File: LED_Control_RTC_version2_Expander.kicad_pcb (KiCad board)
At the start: 4 copper layers, 100 x 60 mm, 90 parts, among them J10 Conn_01x06_Male, J210 Conn_01x02, J220 Conn_01x02, J230 Conn_01x02, J240 Conn_01x02, J250 Conn_01x02, J260 Conn_01x02, J3 Conn_02x04_Odd_Even, J4 DS1023-2*8SF11, J5 DS1023-2*8SF11, J9 Conn_01x06_Male, Q1 IRLR8726TRPBF, Q10 IRLR8726TRPBF, Q2 IRLR8726TRPBF, Q3 IRLR8726TRPBF, Q4 IRLR8726TRPBF, Q5 IRLR8726TRPBF, Q6 IRLR8726TRPBF, Q7 IRLR8726TRPBF, Q8 IRLR8726TRPBF, Q9 IRLR8726TRPBF, U101 TC4427, U102 TC4427, U103 TC4427, U104 TC4427, U105 TC4427

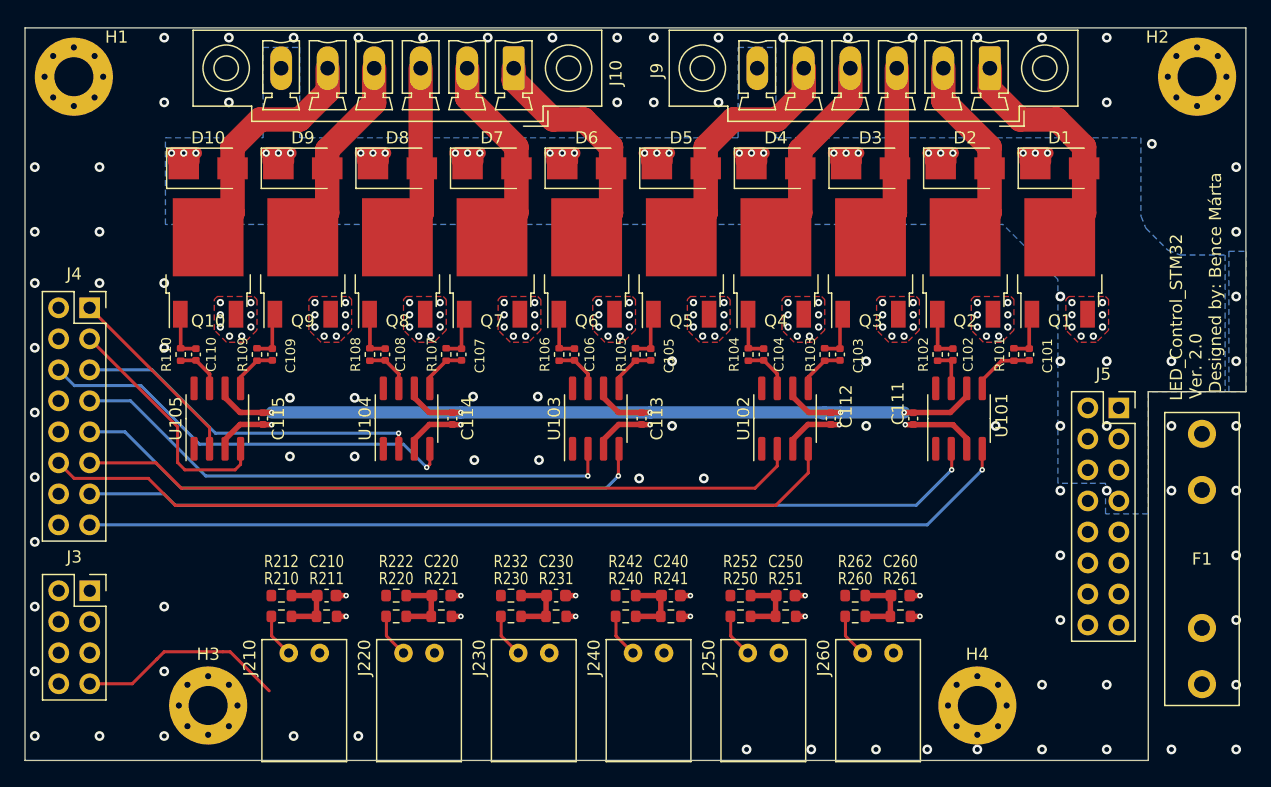
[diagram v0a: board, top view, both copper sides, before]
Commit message: Added ESD protection to switch inputs and filled planes
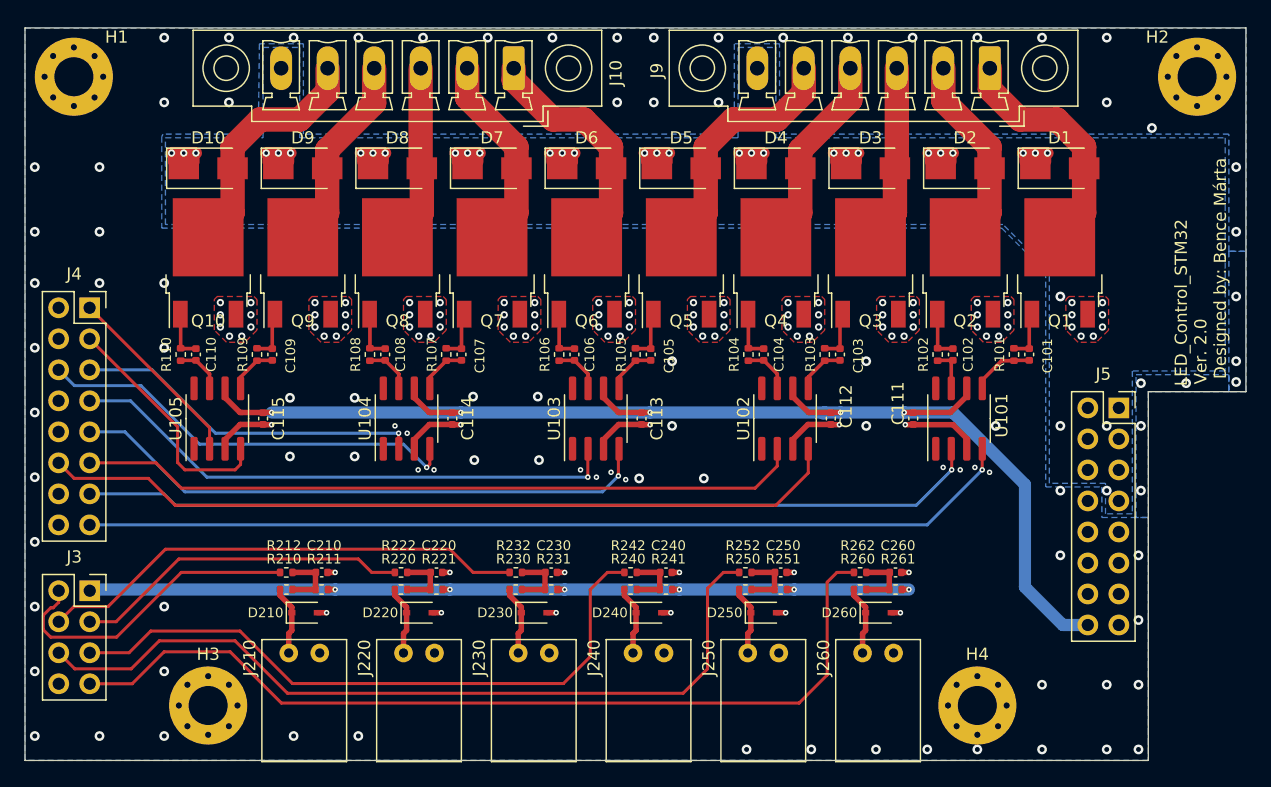
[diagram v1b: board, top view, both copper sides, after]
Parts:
- removed F1: Fuse_Small, Fuse:Fuseholder_Littelfuse_100_series_5x20mm
- added D210: 5V, Diode_SMD:D_SOD-323, F.Cu at (117.9, 102.9)
- added D220: 5V, Diode_SMD:D_SOD-323, F.Cu at (127.3, 102.9)
- added D230: 5V, Diode_SMD:D_SOD-323, F.Cu at (136.7, 102.9)
- added D240: 5V, Diode_SMD:D_SOD-323, F.Cu at (146.1, 102.9)
- added D250: 5V, Diode_SMD:D_SOD-323, F.Cu at (155.5, 102.9)
- added D260: 5V, Diode_SMD:D_SOD-323, F.Cu at (164.9, 102.9)
- C210, C220, C230, C240, C250, C260: value 100n -> 10n; footprint Capacitor_SMD:C_0603_1608Metric -> Capacitor_SMD:C_0402_1005Metric
- R210, R211, R212, R220, R221, R222, R230, R231, R232, R240, R241, R242, R250, R251, R252, R260, R261, R262: footprint Resistor_SMD:R_0603_1608Metric -> Resistor_SMD:R_0402_1005Metric
- moved R210 2.24 mm to (116.4, 101.0)
- moved R211 2.24 mm to (119.3, 101.0)
- moved R221 2.24 mm to (128.7, 101.0)
- moved R231 2.24 mm to (138.1, 101.0)
- moved R240 2.24 mm to (144.6, 101.0)
- moved R241 2.24 mm to (147.5, 101.0)
- moved R250 2.24 mm to (154.0, 101.0)
- moved R251 2.24 mm to (156.9, 101.0)
- moved R260 2.24 mm to (163.4, 101.0)
- moved R220 2.24 mm to (125.8, 101.0)
- moved R230 2.24 mm to (135.2, 101.0)
- moved R261 2.24 mm to (166.3, 101.0)
- moved C210 1.94 mm to (119.3, 99.6)
- moved C220 1.94 mm to (128.7, 99.6)
- moved C230 1.94 mm to (138.1, 99.6)
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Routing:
- net /M2_IO5: track 0.00 -> 67.0 mm
- net +3V3: track 4.65 -> 70.7 mm
- net /M2_IO6: track 17.1 -> 74.3 mm
- net /M2_IO4: track 0.00 -> 53.3 mm
- net /M2_IO3: track 0.00 -> 40.2 mm
- net /M2_IO2: track 0.00 -> 27.6 mm
- net +5V: track 78.7 -> 105.9 mm
- net /M2_IO1: track 0.00 -> 25.7 mm
- net GND: track 31.6 -> 34.9 mm, vias 183 -> 197
- net Net-(J260-Pad1): track 3.59 -> 5.70 mm
- net Net-(J240-Pad1): track 3.59 -> 5.70 mm
- net Net-(J220-Pad1): track 3.59 -> 5.70 mm
- net Net-(J210-Pad1): track 3.59 -> 5.70 mm
- net Net-(J250-Pad1): track 3.59 -> 5.70 mm
- net Net-(J230-Pad1): track 3.59 -> 5.70 mm
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
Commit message: Finished design
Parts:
- added C100: 10u, Resistor_SMD:R_1206_3216Metric, F.Cu at (134.8, 88.9)
- added C200: 100n, Capacitor_SMD:C_0402_1005Metric, F.Cu at (102.8, 98.4)
- added C201: 100n, Capacitor_SMD:C_0402_1005Metric, F.Cu at (169.0, 101.0)
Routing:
- net +3V3: track 70.7 -> 74.1 mm, vias 6 -> 7
- net GND: track 34.9 -> 37.8 mm, vias 197 -> 198
- net +5V: track 105.9 -> 108.1 mm, vias 5 -> 7

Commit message: Ready for prod
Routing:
- net GND: vias 198 -> 202
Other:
- outline, holes or cut-outs redrawn
- board text added: "JLCJLCJLCJLC"
